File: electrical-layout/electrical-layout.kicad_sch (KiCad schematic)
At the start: 0 parts

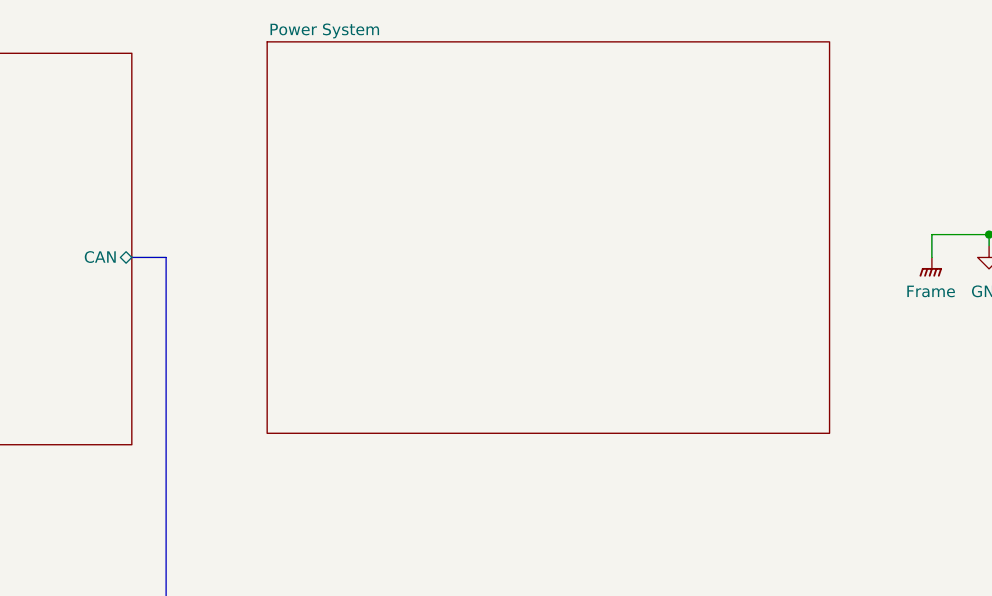
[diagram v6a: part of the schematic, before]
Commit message: layout-2025: add power control pcb
This PCB is used to:
- Control power MOSFETs (as switches)
- Read UART data from fuel cell(s) and charge controller
- Communicate over the CAN bus

Unknown switches were replaced with MOSFETs in the power layout.
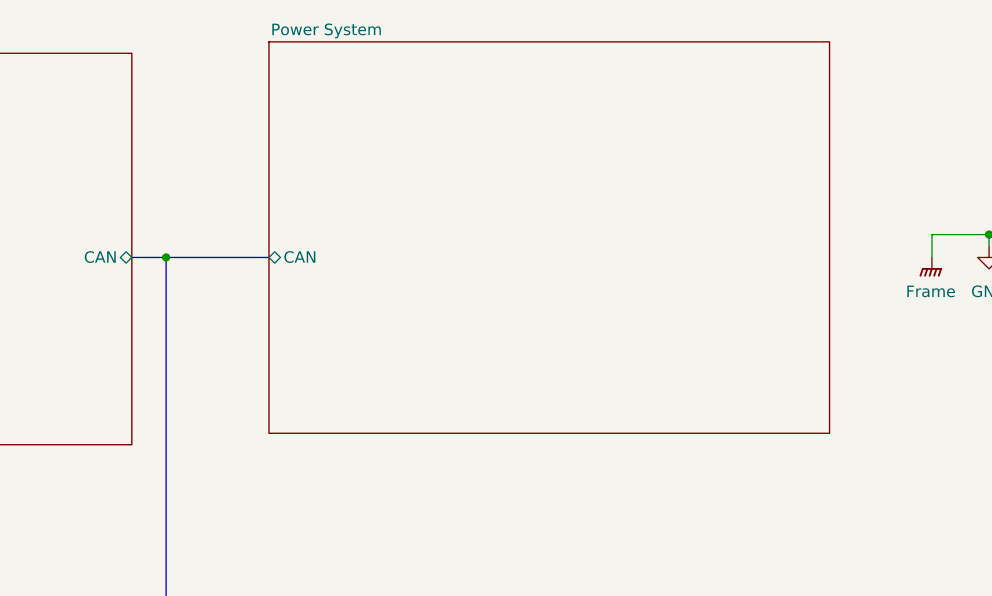
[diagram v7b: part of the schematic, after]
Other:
- sheet Power System ports: added CAN; removed none
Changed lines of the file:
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@@
+	)
+	(junction
+		(at 83.82 43.18)
+		(diameter 0)
+		(color 0 0 0 0)
 	)
 	(junction
@@
 		(pts
 			(xy 80.01 90.17) (xy 83.82 90.17)
+		)
+		(stroke
+			(width 0)
+			(type default)
+		)
+	)
+	(bus
+		(pts
+			(xy 83.82 43.18) (xy 95.25 43.18)
 		)
 		(stroke
@@
 	)
 	(sheet
-		(at 95.0484 19.2259)
-		(size 62.4875 43.4913)
+		(at 95.25 19.2259)
+		(size 62.2859 43.4913)
 		(exclude_from_sim no)
 		(in_bom yes)
@@
 		)
 		(property "Sheetname" "Power System"
-			(at 95.25 17.145 0)
+			(at 95.4516 17.145 0)
 			(effects
 				(font
@@
 		)
 		(property "Sheetfile" "power_system.kicad_sch"
-			(at 95.25 63.5 0)
-			(effects
-				(font
-					(size 1.27 1.27)
-				)
-				(justify left top)
-				(hide yes)
-			)
-		)
+			(at 95.4516 63.5 0)
+			(effects
+				(font
+					(size 1.27 1.27)
+				)
+				(justify left top)
+				(hide yes)
+			)
+		)
+		(pin "CAN" bidirectional
+			(at 95.25 43.18 180)
+			(effects
+				(font
+					(size 1.27 1.27)
+				)
+				(justify left)
+			)
+		)
